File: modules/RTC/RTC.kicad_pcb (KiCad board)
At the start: 2 copper layers, 40.6 x 40.6 mm, 26 parts, among them J1 2, J10 11, J11 12, J12 13, J13 A0, J14 A1, J15 A2, J16 A3, J17 A4, J18 A5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

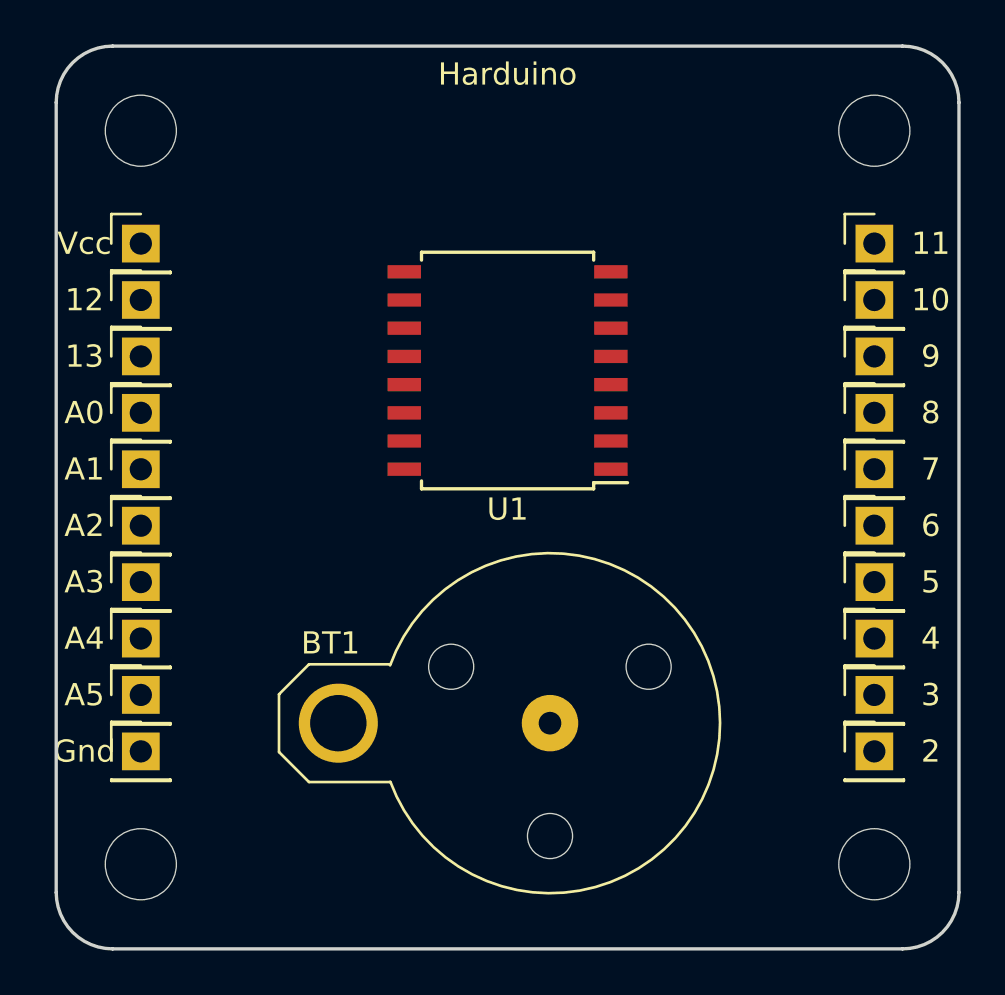
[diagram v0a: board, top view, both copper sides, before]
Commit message: RTC pcb + CR1220 holder
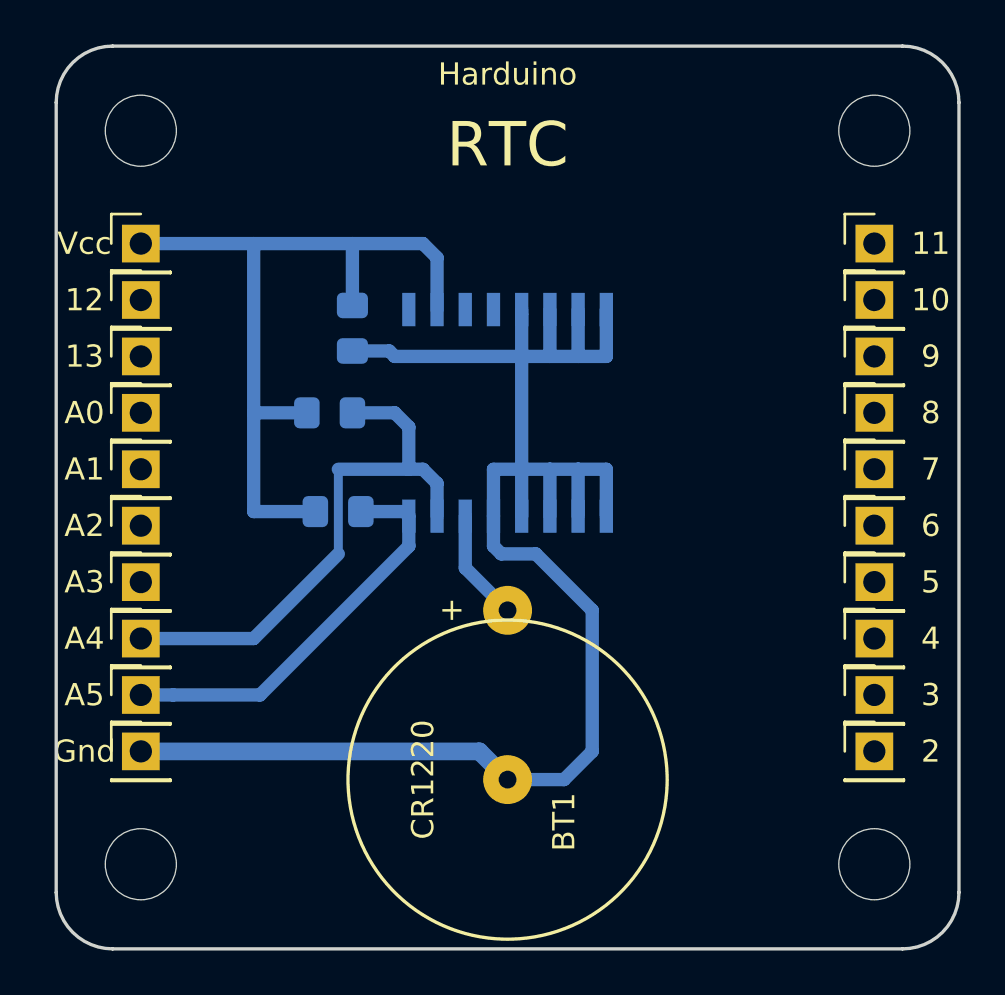
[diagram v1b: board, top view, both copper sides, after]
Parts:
- added C1: 0,1uF, Capacitor_SMD:C_0805_2012Metric_Pad1.15x1.40mm_HandSolder, B.Cu at (102.2, 63.5)
- added R1: 10k, Resistor_SMD:R_0805_2012Metric_Pad1.15x1.40mm_HandSolder, B.Cu at (101.2, 67.3)
- added R2: 10k, Resistor_SMD:R_0805_2012Metric_Pad1.15x1.40mm_HandSolder, B.Cu at (101.6, 71.8)
- BT1: footprint Battery:BatteryHolder_Keystone_500 -> CommonLibrary:CR1220-holder
- U1: moved to B.Cu
- moved BT1 8.03 mm to (109.2, 83.8), turned to 270 degrees
- moved U1 1.91 mm to (109.2, 67.3), turned to 270 degrees
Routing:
- net GND: track 0.00 -> 75.4 mm
- net VCC: track 0.00 -> 35.9 mm
- net Net-(J17-Pad1): track 0.00 -> 25.2 mm
- net Net-(J18-Pad1): track 0.00 -> 18.5 mm
- net Net-(BT1-Pad1): track 0.00 -> 5.03 mm
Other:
- board text added: "DS3231"
- board text added: "RTC"

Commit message: Add silk
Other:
- board text added: "SCL"
- board text added: "SDA"
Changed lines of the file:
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@@
   (general
     (thickness 1.6)
-    (drawings 31)
+    (drawings 33)
     (tracks 58)
     (zones 0)
@@
   )
   (setup
-    (last_trace_width 0.6)
+    (last_trace_width 0.25)
     (user_trace_width 0.6)
     (user_trace_width 0.8)
@@
     )
   )
+  (gr_text SCL (at 96.2025 80.01) (layer F.SilkS)
+    (effects (font (size 1 1) (thickness 0.15)))
+  )
+  (gr_text SDA (at 96.2025 77.47) (layer F.SilkS)
+    (effects (font (size 1 1) (thickness 0.15)))
+  )
   (gr_text RTC (at 109.22 55.245) (layer F.SilkS)

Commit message: Harduino -> HardDuino
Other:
- board text added: "HardDuino"
- board text removed: "Harduino"
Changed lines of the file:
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@@
     (effects (font (size 1 1) (thickness 0.15)) (justify mirror))
   )
-  (gr_text Harduino (at 109.22 52.07) (layer F.SilkS)
+  (gr_text HardDuino (at 109.22 52.07) (layer F.SilkS)
     (effects (font (size 1 1) (thickness 0.15)))
   )
